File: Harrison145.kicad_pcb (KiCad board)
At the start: 2 copper layers, 85 x 55 mm, 150 parts, among them J1 PITCH ANTENNA, J2 VOLUME ANTENNA, J3 GROUND POINT, J4 LINE OUT, J5 9V IN, Q1 MMBT3906, Q10 SMP5484, Q11 MMBT3906, Q12 MMBT3906, Q13 SMP5484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

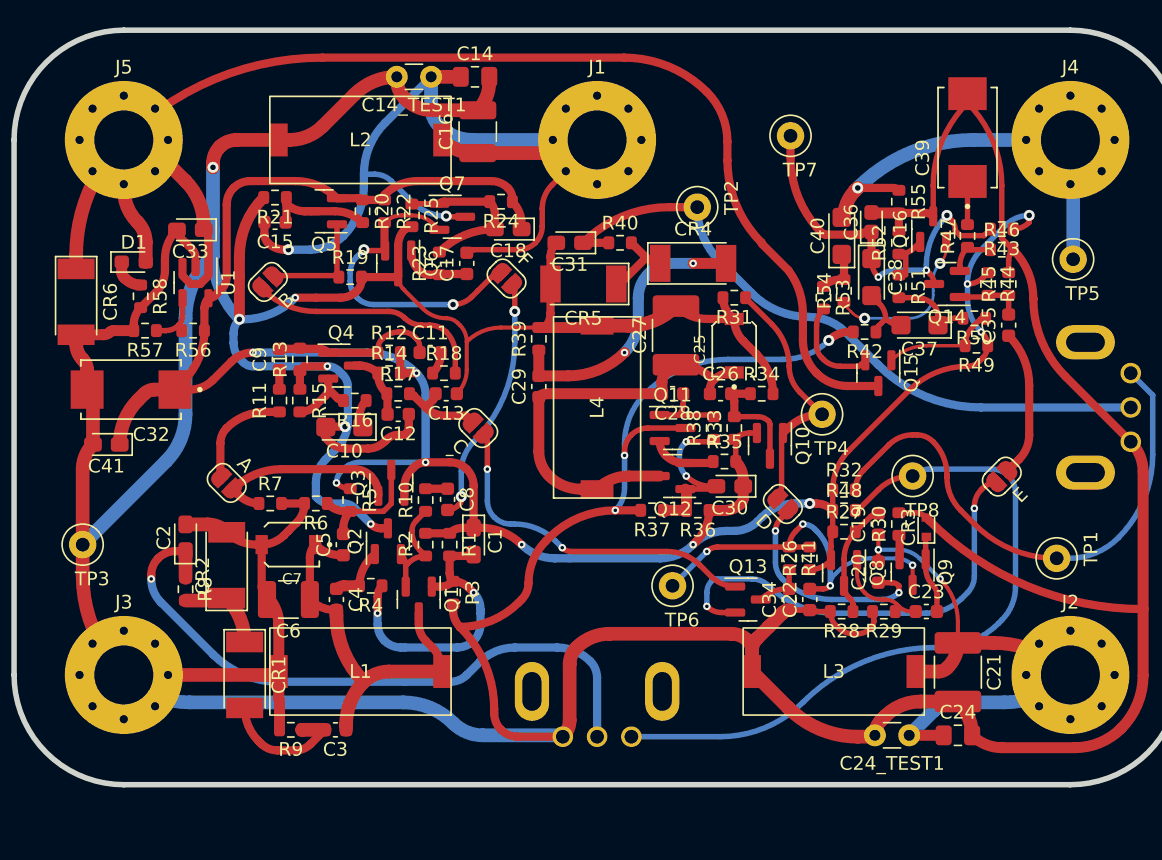
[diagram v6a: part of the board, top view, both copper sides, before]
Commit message: Reduced silk designators; DRC passes
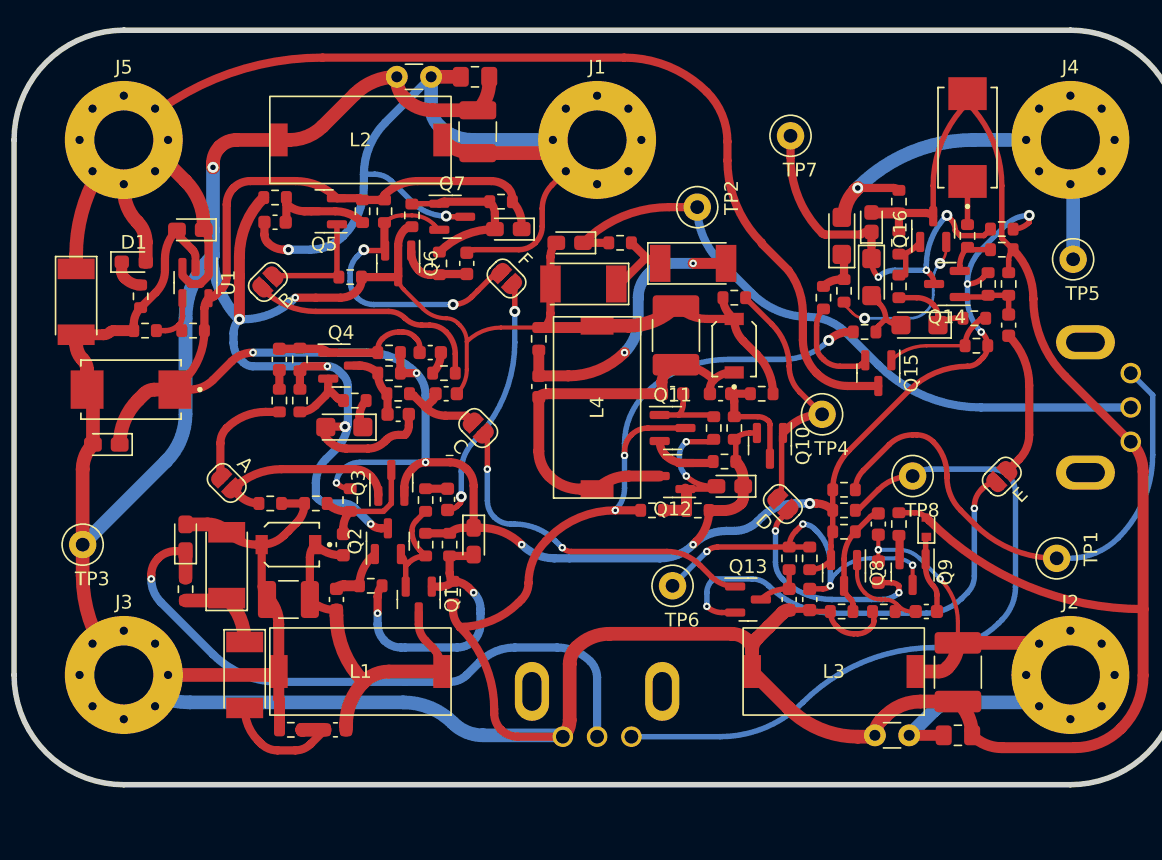
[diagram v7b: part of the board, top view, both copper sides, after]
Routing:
- net Net-(C40-Pad2): track 30.6 -> 24.2 mm
- net Net-(C19-Pad1): track 41.1 -> 35.0 mm

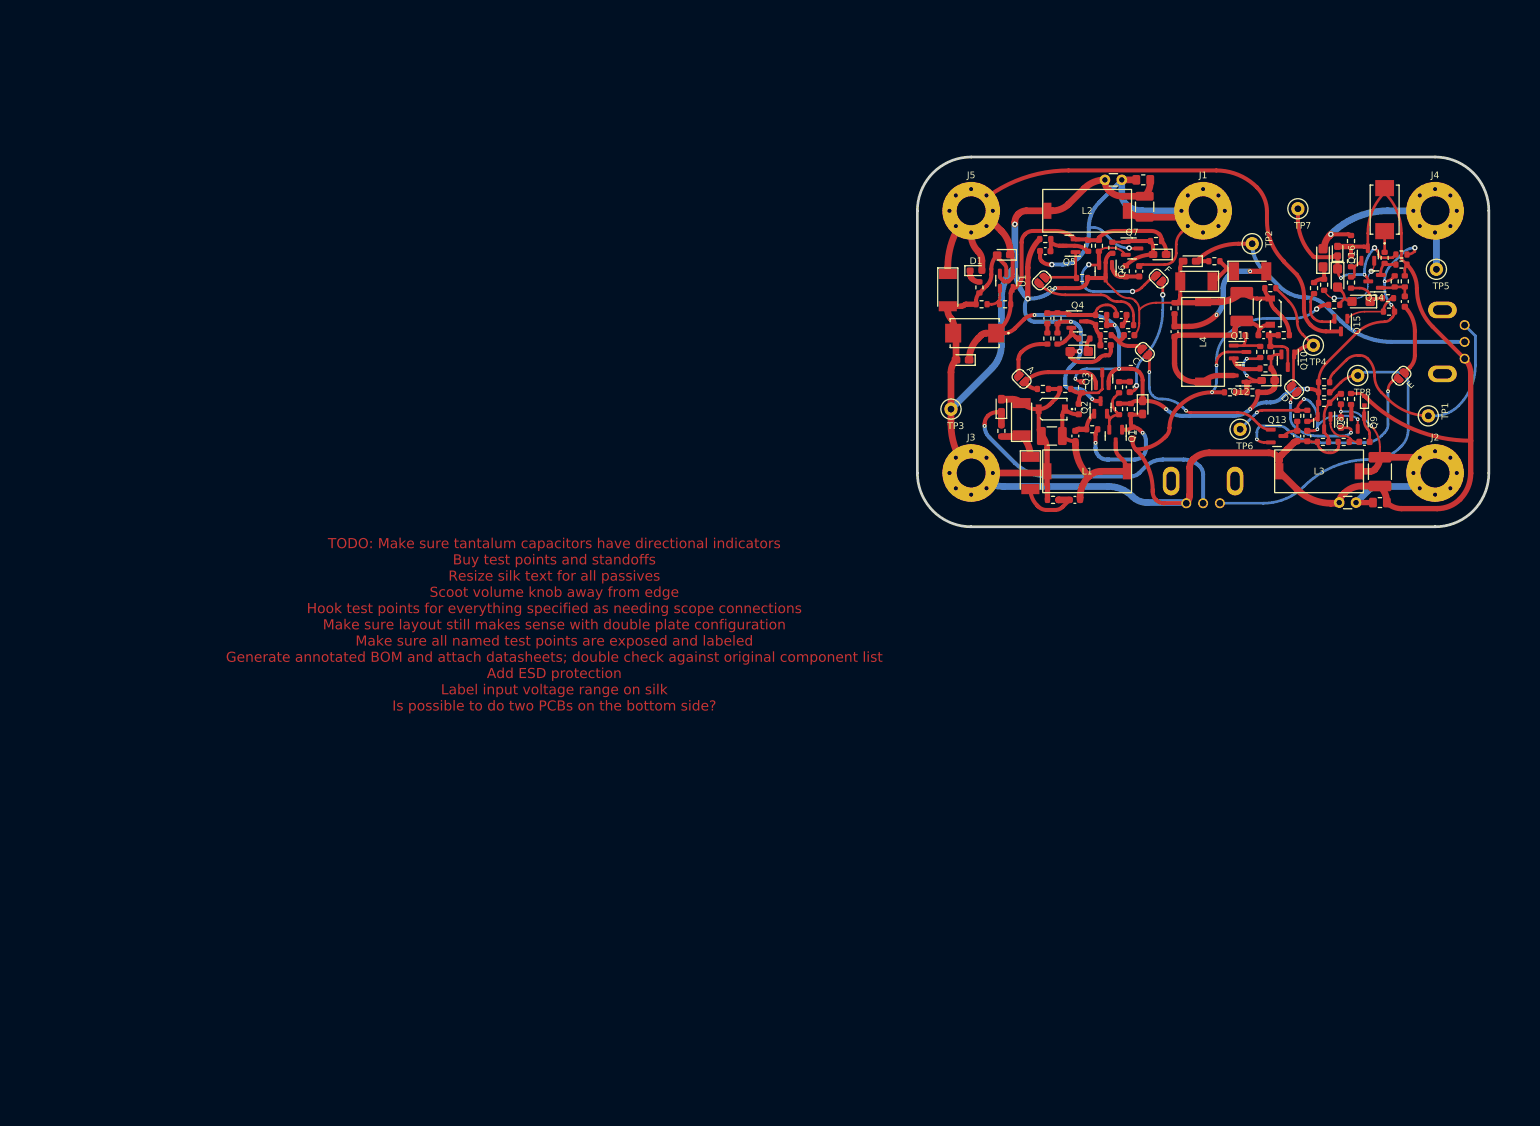
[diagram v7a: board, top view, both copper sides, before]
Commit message: Added aseprite backgrounds
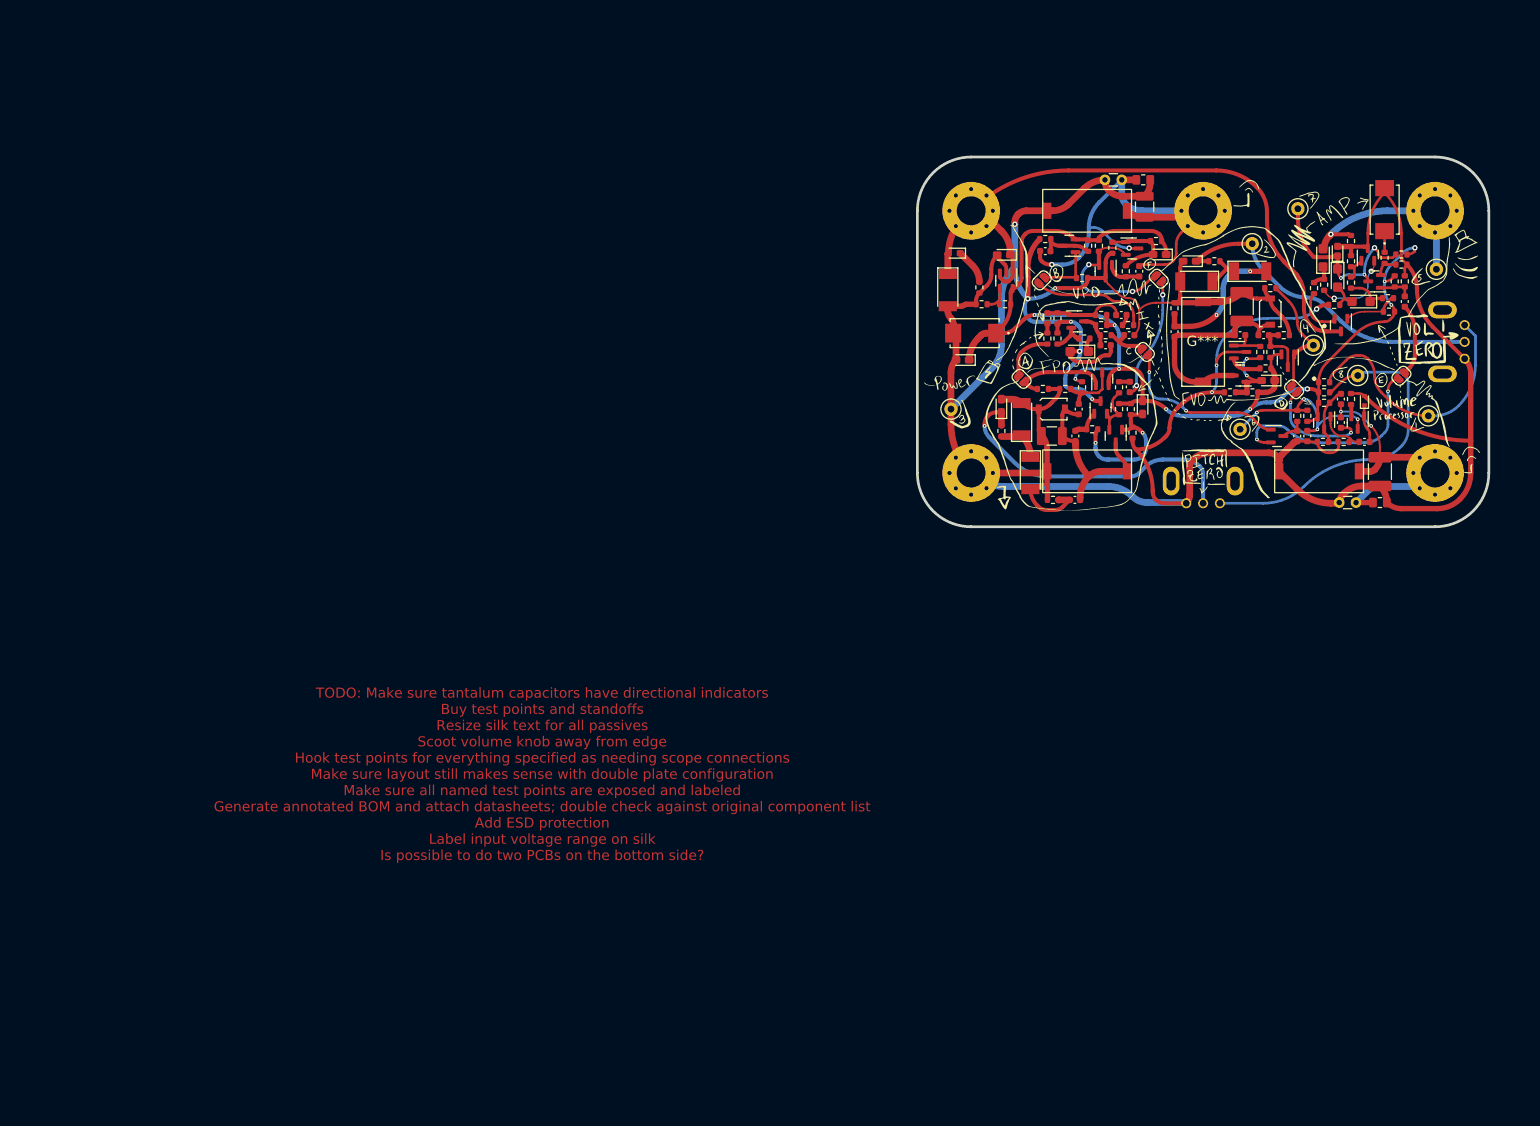
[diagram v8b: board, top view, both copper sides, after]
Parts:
- added G***: LOGO, Theremin:FrontSilk, F.Cu at (182.9, 79.4)
- added G***: LOGO, Theremin:RearSilk, B.Cu at (183.3, 79.4)
- moved D1 4.14 mm to (146.0, 66.3), turned to 180 degrees
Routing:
- net +9V: track 106.4 -> 97.3 mm
- net Net-(D1-Pad1): track 2.53 -> 5.29 mm
